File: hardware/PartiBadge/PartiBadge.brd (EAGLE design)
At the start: 101.6 x 101.6 mm, 21 parts, among them J1 I2C, J2 Supply

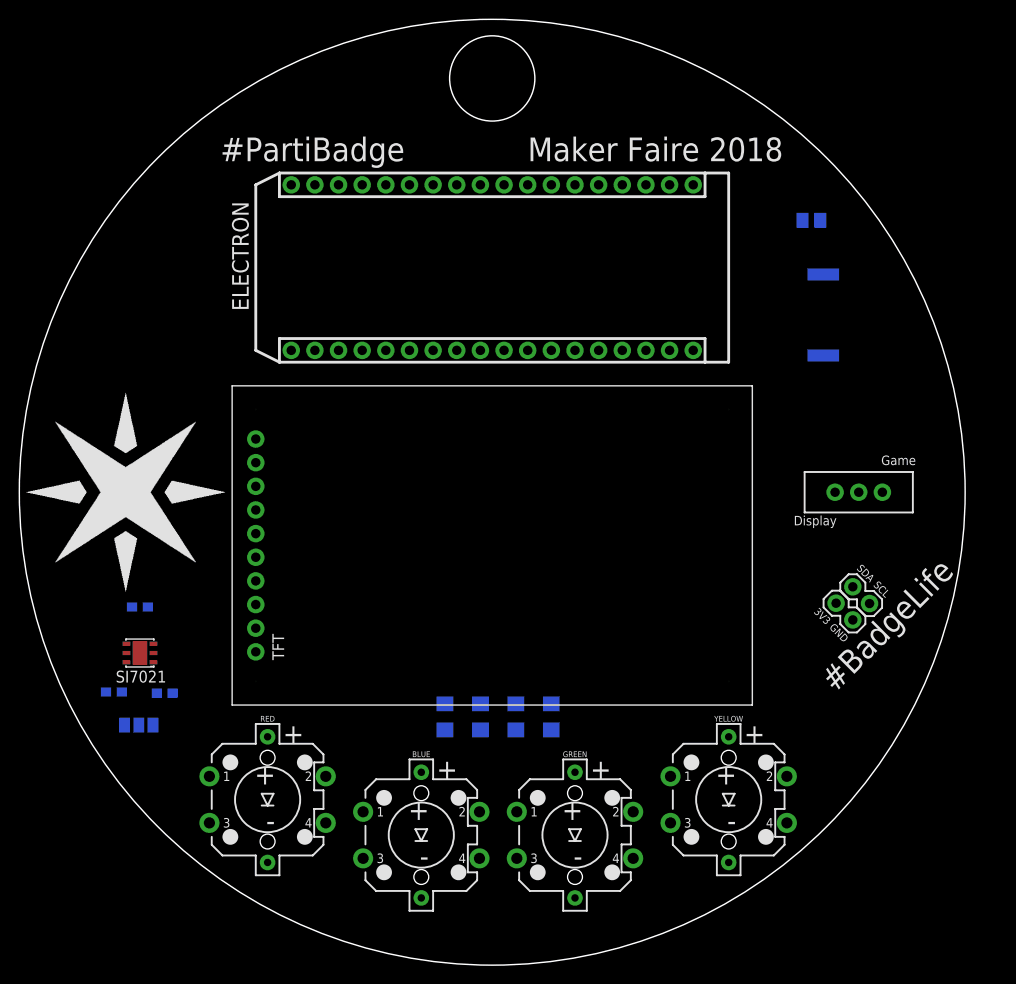
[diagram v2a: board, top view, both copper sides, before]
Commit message: added frame and cleaned up schematic; added 5-way joystick
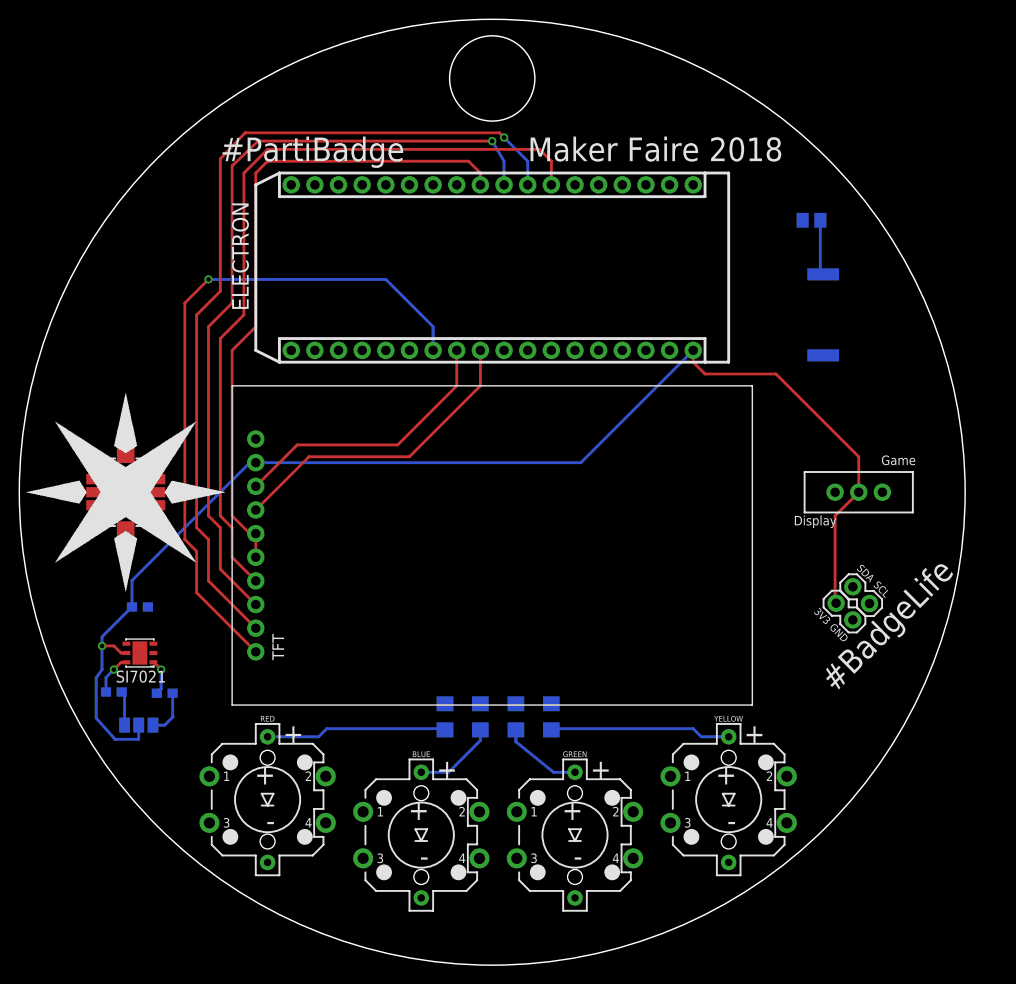
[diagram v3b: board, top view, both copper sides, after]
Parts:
- added PARTIFRAME: FRAME-LETTERNO_PACKAGE, SparkFun-Aesthetics:DUMMY
- added S1: (no value), SparkFun-Switches:JOYSTICK_MINI
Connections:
- new net CENT: ELECTRON.32, S1.CTR
- new net DOWN: ELECTRON.31, S1.D
- new net LEFT: ELECTRON.4, S1.C
- new net RIGHT: ELECTRON.3, S1.B
- new net UP: ELECTRON.30, S1.A
- net GND: now also S1.GND
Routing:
- net 3V3: track 0.00 -> 137.0 mm, vias 0 -> 1
- net SPI_MISO: track 0.00 -> 92.1 mm, vias 0 -> 1
- net SPI_SCK: track 0.00 -> 84.3 mm, vias 0 -> 1
- net SPI_MOSI: track 0.00 -> 83.6 mm
- net TFT_LITE: track 0.00 -> 73.0 mm, vias 0 -> 1
- net SPI_SS: track 0.00 -> 70.2 mm
- net SPI_DC: track 0.00 -> 33.5 mm
- net TFT_RST: track 0.00 -> 29.9 mm
- net N$4: track 0.00 -> 19.5 mm
- net N$10: track 0.00 -> 19.5 mm
- net N$8: track 0.00 -> 8.90 mm
- net N$7: track 0.00 -> 8.78 mm
- net N$13: track 0.00 -> 5.94 mm
- net N$11: track 0.00 -> 5.08 mm
- net SCL: track 0.00 -> 4.43 mm, vias 0 -> 1
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
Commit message: routed board. closes #3 and #4
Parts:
- moved U$2 15.5 mm to (16.5, 72.4)
- moved R4 11.5 mm to (71.1, 31.8), flipped to the top, turned to 0 degrees
- moved S5 9.25 mm to (90.2, 66.0)
- moved R1 8.98 mm to (39.4, 31.8), flipped to the top, turned to 180 degrees
- moved R2 5.24 mm to (61.0, 31.8), flipped to the top, turned to 0 degrees
- moved R3 5.24 mm to (47.0, 31.8), flipped to the top, turned to 180 degrees
- moved S1 4.58 mm to (11.4, 53.3), turned to 315 degrees
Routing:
- net N$9: track 0.00 -> 206.5 mm
- net LED_BLUE: track 0.00 -> 179.3 mm
- net LED_GREEN: track 0.00 -> 157.8 mm, vias 0 -> 1
- net SCL: track 4.43 -> 146.7 mm, vias 1 -> 3
- net N$6: track 0.00 -> 136.8 mm
- net SDA: track 3.89 -> 122.7 mm, vias 1 -> 3
- net N$1: track 0.00 -> 101.5 mm
- net LEFT: track 0.00 -> 88.8 mm, vias 0 -> 1
- net RIGHT: track 0.00 -> 86.3 mm, vias 0 -> 1
- net DOWN: track 0.00 -> 84.2 mm, vias 0 -> 1
- net N$5: track 0.00 -> 74.4 mm, vias 0 -> 1
- net CENT: track 0.00 -> 71.6 mm, vias 0 -> 1
- net LED_RED: track 0.00 -> 71.6 mm, vias 0 -> 2
- net UP: track 0.00 -> 63.8 mm, vias 0 -> 1
- net N$2: track 0.00 -> 63.2 mm, vias 0 -> 2
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- added copper zone on layer 16, net GND

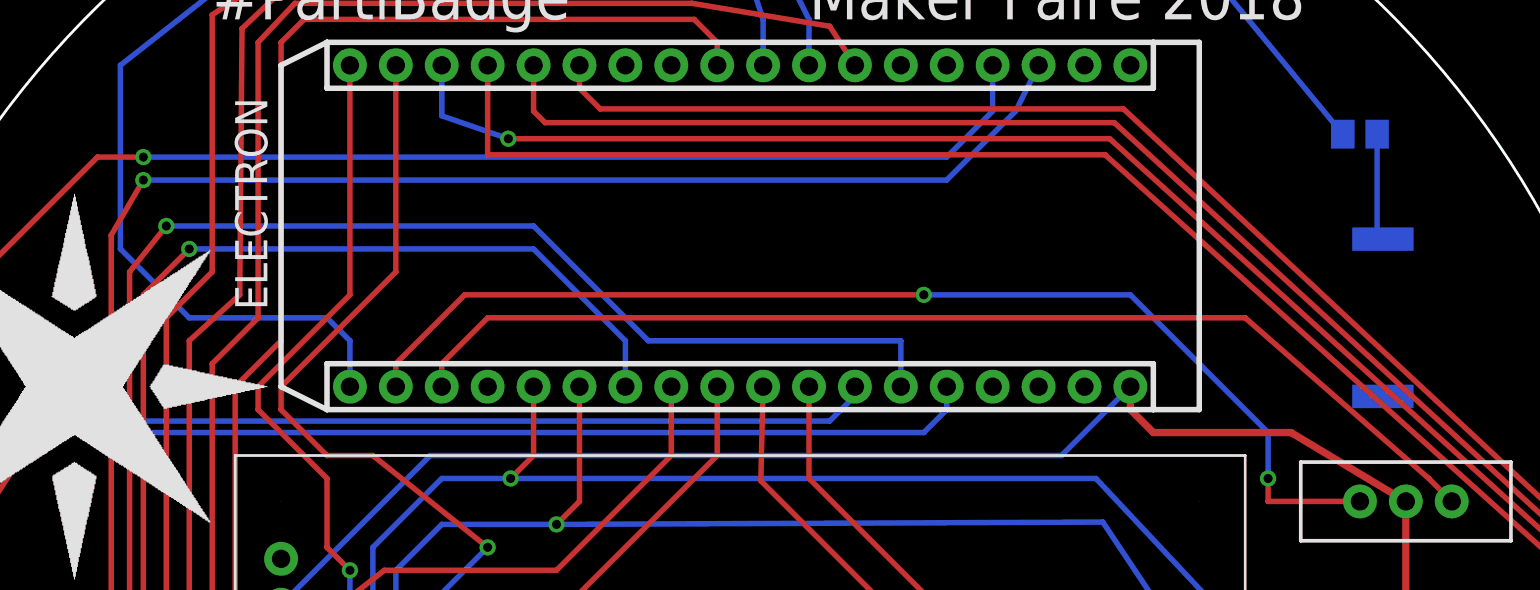
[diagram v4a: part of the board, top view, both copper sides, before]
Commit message: added slot for lipo and antenna; closes #7
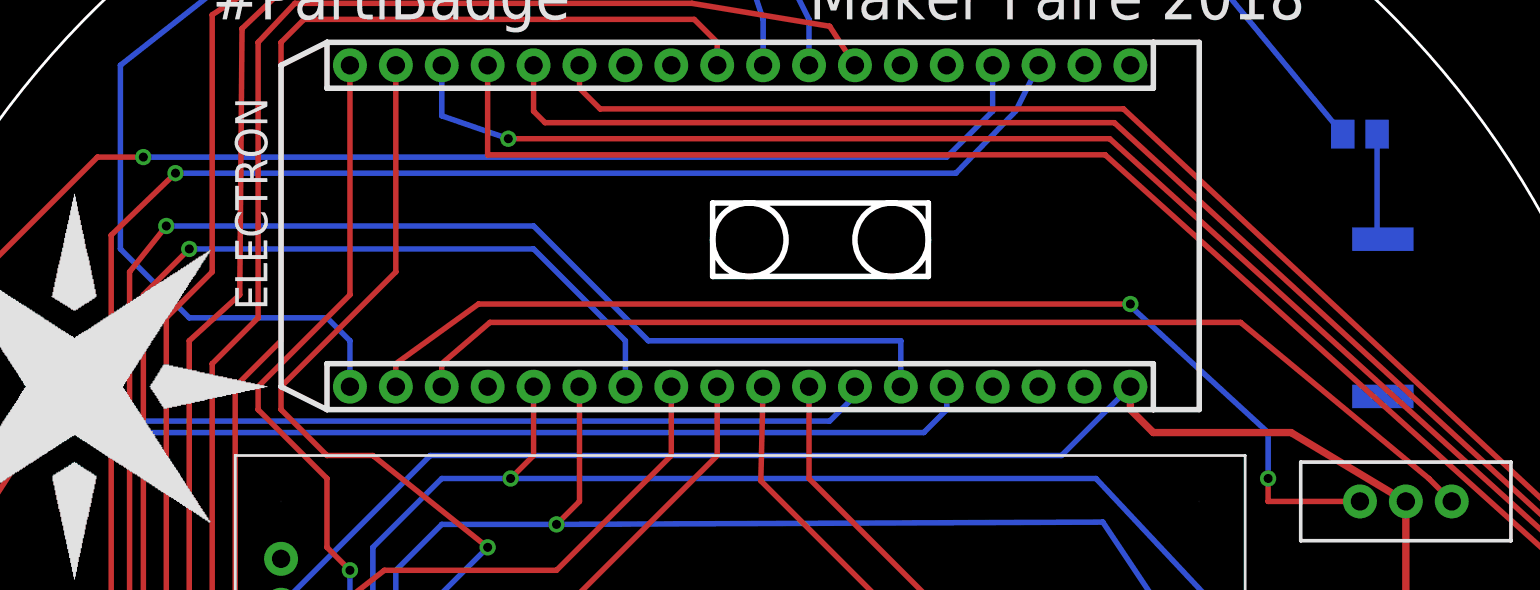
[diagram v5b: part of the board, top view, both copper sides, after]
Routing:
- net N$2: track 63.2 -> 62.5 mm
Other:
- outline, holes or cut-outs redrawn
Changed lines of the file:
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@@
 <layer number="44" name="Drills" color="7" fill="1" visible="no" active="yes"/>
 <layer number="45" name="Holes" color="7" fill="1" visible="yes" active="yes"/>
-<layer number="46" name="Milling" color="3" fill="1" visible="no" active="yes"/>
+<layer number="46" name="Milling" color="3" fill="1" visible="yes" active="yes"/>
 <layer number="47" name="Measures" color="7" fill="1" visible="no" active="yes"/>
 <layer number="48" name="Document" color="7" fill="1" visible="yes" active="yes"/>
@@
 <hole x="78.74" y="66.04" drill="0.0022"/>
 <hole x="27.94" y="36.83" drill="0.0022"/>
+<circle x="53.848" y="80.518" radius="2.032" width="0.3048" layer="20"/>
+<circle x="61.722" y="80.518" radius="2.032" width="0.3048" layer="20"/>
+<wire x1="51.816" y1="82.55" x2="63.754" y2="82.55" width="0.3048" layer="46"/>
+<wire x1="51.816" y1="82.55" x2="51.816" y2="78.486" width="0.3048" layer="46"/>
+<wire x1="51.816" y1="78.486" x2="63.754" y2="78.486" width="0.3048" layer="46"/>
+<wire x1="63.754" y1="78.486" x2="63.754" y2="82.55" width="0.3048" layer="46"/>
 </plain>
 <attributes>
@@
 <via x="82.55" y="67.31" extent="1-16" drill="0.5"/>
 <wire x1="82.55" y1="67.31" x2="82.55" y2="69.85" width="0.3048" layer="16"/>
-<wire x1="82.55" y1="69.85" x2="74.93" y2="77.47" width="0.3048" layer="16"/>
-<wire x1="74.93" y1="77.47" x2="63.5" y2="77.47" width="0.3048" layer="16"/>
-<via x="63.5" y="77.47" extent="1-16" drill="0.5"/>
-<wire x1="63.5" y1="77.47" x2="38.1" y2="77.47" width="0.3048" layer="1"/>
-<wire x1="38.1" y1="77.47" x2="34.29" y2="73.66" width="0.3048" layer="1"/>
+<wire x1="82.55" y1="69.85" x2="74.803" y2="76.962" width="0.3048" layer="16"/>
+<wire x1="74.803" y1="76.962" x2="74.93" y2="76.962" width="0.3048" layer="16"/>
+<via x="74.93" y="76.962" extent="1-16" drill="0.5"/>
+<wire x1="74.93" y1="76.962" x2="38.862" y2="76.962" width="0.3048" layer="1"/>
+<wire x1="38.862" y1="76.962" x2="34.29" y2="73.66" width="0.3048" layer="1"/>
 <wire x1="34.29" y1="73.66" x2="34.29" y2="72.39" width="0.3048" layer="1"/>
 </signal>
@@
 <contactref element="ELECTRON" pad="21"/>
 <wire x1="92.71" y1="66.04" x2="91.44" y2="67.31" width="0.3048" layer="1"/>
-<wire x1="91.44" y1="67.31" x2="81.28" y2="76.2" width="0.3048" layer="1"/>
-<wire x1="81.28" y1="76.2" x2="39.37" y2="76.2" width="0.3048" layer="1"/>
-<wire x1="39.37" y1="76.2" x2="36.83" y2="73.66" width="0.3048" layer="1"/>
+<wire x1="91.44" y1="67.31" x2="81.026" y2="75.946" width="0.3048" layer="1"/>
+<wire x1="81.026" y1="75.946" x2="39.497" y2="75.946" width="0.3048" layer="1"/>
+<wire x1="39.497" y1="75.946" x2="36.83" y2="73.66" width="0.3048" layer="1"/>
 <wire x1="36.83" y1="73.66" x2="36.83" y2="72.39" width="0.3048" layer="1"/>
 </signal>
@@
 <contactref element="S1" pad="B"/>
 <contactref element="ELECTRON" pad="3"/>
-<via x="20.32" y="83.82" extent="1-16" drill="0.5"/>
-<wire x1="20.32" y1="83.82" x2="64.77" y2="83.82" width="0.3048" layer="16"/>
-<wire x1="64.77" y1="83.82" x2="68.58" y2="87.63" width="0.3048" layer="16"/>
+<via x="22.098" y="84.201" extent="1-16" drill="0.5"/>
+<wire x1="22.098" y1="84.201" x2="65.278" y2="84.201" width="0.3048" layer="16"/>
+<wire x1="65.278" y1="84.201" x2="68.58" y2="87.63" width="0.3048" layer="16"/>
 <wire x1="68.58" y1="87.63" x2="69.85" y2="90.17" width="0.3048" layer="16"/>
 <wire x1="14.771078125" y1="51.97881875" x2="18.542" y2="57.019740625" width="0.3048" layer="1"/>
 <wire x1="18.542" y1="57.019740625" x2="18.542" y2="80.772" width="0.3048" layer="1"/>
-<wire x1="18.542" y1="80.772" x2="20.32" y2="83.82" width="0.3048" layer="1"/>
+<wire x1="18.542" y1="80.772" x2="22.098" y2="84.201" width="0.3048" layer="1"/>
 </signal>
 <signal name="CENT">
@@
 </signal>
 </signals>
+<errors>
+</errors>
 </board>
 </drawing>
